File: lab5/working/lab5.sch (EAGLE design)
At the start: 29 parts, among them J1 ISP, U1 ATMEGA128RFA1, Y1 16MHz

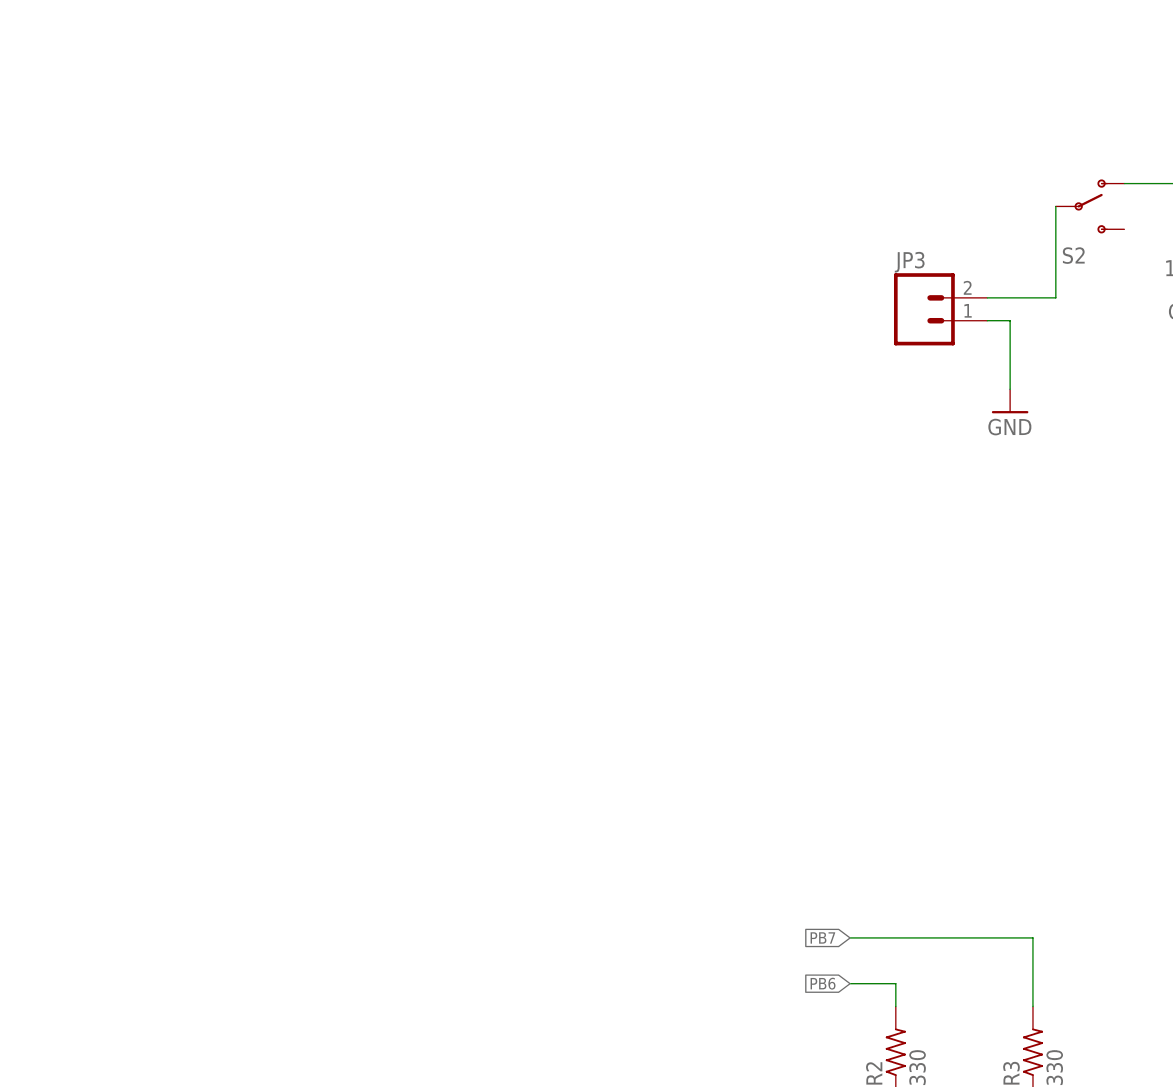
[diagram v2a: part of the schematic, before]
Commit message: added power IMU
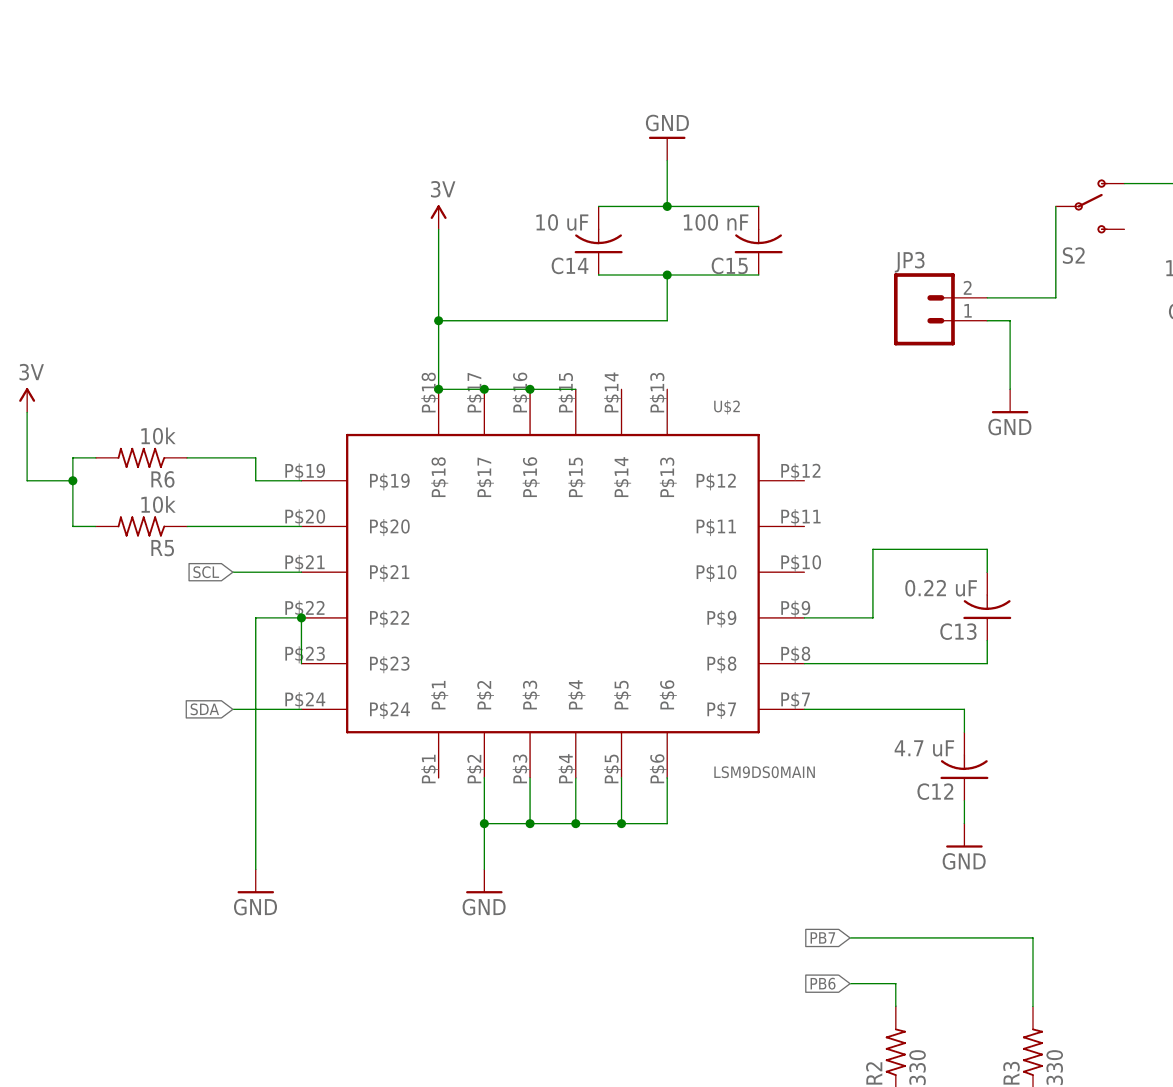
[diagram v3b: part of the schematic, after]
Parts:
- added C12: 4.7 uF, Lab5:C-USC0805
- added C13: 0.22 uF, Lab5:C-USC0805
- added C14: 10 uF, Lab5:C-USC0805
- added C15: 100 nF, Lab5:C-USC0805
- added R5, R6: 10k, Lab5:R-US_R0805
- added U$2: LSM9DS0MAIN, lab4:LSM9DS0MAIN
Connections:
- new net N$21: C12.2, U$2.P$7
- new net N$22: C13.2, U$2.P$9
- new net N$23: C13.1, U$2.P$8
- new net N$28: R5.1, U$2.P$20
- new net N$29: R6.1, U$2.P$19
- net 3.3V: now also C14.1, C15.1, R5.2, R6.2, U$2.P$15, U$2.P$16, U$2.P$17, U$2.P$18
- net GND: now also C12.1, C14.2, C15.2, U$2.P$2, U$2.P$22, U$2.P$23, U$2.P$3, U$2.P$4, U$2.P$5, U$2.P$6
- net SCL: now also U$2.P$21
- net SDA: now also U$2.P$24
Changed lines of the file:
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@@
 <part name="GND20" library="Lab5" deviceset="GND" device=""/>
 <part name="R4" library="Lab5" deviceset="R-US_" device="R0805" value="1k"/>
+<part name="U$2" library="lab4" deviceset="LSM9DS0" device="MAIN"/>
+<part name="P+4" library="Lab5" deviceset="3.3V" device="" value="3V"/>
+<part name="GND21" library="Lab5" deviceset="GND" device=""/>
+<part name="C12" library="Lab5" deviceset="C-US" device="C0805" value="4.7 uF"/>
+<part name="GND22" library="Lab5" deviceset="GND" device=""/>
+<part name="C13" library="Lab5" deviceset="C-US" device="C0805" value="0.22 uF"/>
+<part name="C14" library="Lab5" deviceset="C-US" device="C0805" value="10 uF"/>
+<part name="C15" library="Lab5" deviceset="C-US" device="C0805" value="100 nF"/>
+<part name="GND23" library="Lab5" deviceset="GND" device=""/>
+<part name="GND24" library="Lab5" deviceset="GND" device=""/>
+<part name="R5" library="Lab5" deviceset="R-US_" device="R0805" value="10k"/>
+<part name="R6" library="Lab5" deviceset="R-US_" device="R0805" value="10k"/>
+<part name="P+5" library="Lab5" deviceset="3.3V" device="" value="3V"/>
 </parts>
 <sheets>
@@
 <instance part="GND20" gate="1" x="-30.48" y="30.48"/>
 <instance part="R4" gate="G$1" x="-38.1" y="53.34" rot="R180"/>
+<instance part="U$2" gate="IMU" x="-165.1" y="7.62"/>
+<instance part="P+4" gate="G$1" x="-177.8" y="48.26"/>
+<instance part="GND21" gate="1" x="-172.72" y="-25.4"/>
+<instance part="C12" gate="G$1" x="-119.38" y="-12.7" rot="R180"/>
+<instance part="GND22" gate="1" x="-119.38" y="-20.32"/>
+<instance part="C13" gate="G$1" x="-116.84" y="5.08" rot="R180"/>
+<instance part="C14" gate="G$1" x="-160.02" y="45.72" rot="R180"/>
+<instance part="C15" gate="G$1" x="-142.24" y="45.72" rot="R180"/>
+<instance part="GND23" gate="1" x="-152.4" y="58.42" rot="R180"/>
+<instance part="GND24" gate="1" x="-198.12" y="-25.4"/>
+<instance part="R5" gate="G$1" x="-210.82" y="15.24" rot="R180"/>
+<instance part="R6" gate="G$1" x="-210.82" y="22.86" rot="R180"/>
+<instance part="P+5" gate="G$1" x="-223.52" y="27.94"/>
 </instances>
 <busses>
@@
 <wire x1="-30.48" y1="38.1" x2="-30.48" y2="33.02" width="0.1524" layer="91"/>
 </segment>
+<segment>
+<pinref part="U$2" gate="IMU" pin="P$6"/>
+<wire x1="-152.4" y1="-12.7" x2="-152.4" y2="-17.78" width="0.1524" layer="91"/>
+<pinref part="U$2" gate="IMU" pin="P$5"/>
+<wire x1="-157.48" y1="-12.7" x2="-157.48" y2="-17.78" width="0.1524" layer="91"/>
+<wire x1="-152.4" y1="-17.78" x2="-157.48" y2="-17.78" width="0.1524" layer="91"/>
+<pinref part="U$2" gate="IMU" pin="P$4"/>
+<wire x1="-162.56" y1="-12.7" x2="-162.56" y2="-17.78" width="0.1524" layer="91"/>
+<wire x1="-157.48" y1="-17.78" x2="-162.56" y2="-17.78" width="0.1524" layer="91"/>
+<junction x="-157.48" y="-17.78"/>
+<pinref part="U$2" gate="IMU" pin="P$3"/>
+<wire x1="-167.64" y1="-12.7" x2="-167.64" y2="-17.78" width="0.1524" layer="91"/>
+<wire x1="-162.56" y1="-17.78" x2="-167.64" y2="-17.78" width="0.1524" layer="91"/>
+<junction x="-162.56" y="-17.78"/>
+<pinref part="U$2" gate="IMU" pin="P$2"/>
+<wire x1="-172.72" y1="-12.7" x2="-172.72" y2="-17.78" width="0.1524" layer="91"/>
+<wire x1="-167.64" y1="-17.78" x2="-172.72" y2="-17.78" width="0.1524" layer="91"/>
+<junction x="-167.64" y="-17.78"/>
+<pinref part="GND21" gate="1" pin="GND"/>
+<wire x1="-172.72" y1="-17.78" x2="-172.72" y2="-22.86" width="0.1524" layer="91"/>
+<junction x="-172.72" y="-17.78"/>
+</segment>
+<segment>
+<pinref part="C12" gate="G$1" pin="1"/>
+<pinref part="GND22" gate="1" pin="GND"/>
+<wire x1="-119.38" y1="-15.24" x2="-119.38" y2="-17.78" width="0.1524" layer="91"/>
+</segment>
+<segment>
+<pinref part="C15" gate="G$1" pin="2"/>
+<pinref part="C14" gate="G$1" pin="2"/>
+<wire x1="-142.24" y1="50.8" x2="-152.4" y2="50.8" width="0.1524" layer="91"/>
+<wire x1="-152.4" y1="50.8" x2="-160.02" y2="50.8" width="0.1524" layer="91"/>
+<wire x1="-152.4" y1="50.8" x2="-152.4" y2="55.88" width="0.1524" layer="91"/>
+<junction x="-152.4" y="50.8"/>
+<pinref part="GND23" gate="1" pin="GND"/>
+</segment>
+<segment>
+<pinref part="U$2" gate="IMU" pin="P$23"/>
+<pinref part="U$2" gate="IMU" pin="P$22"/>
+<wire x1="-193.04" y1="0" x2="-193.04" y2="5.08" width="0.1524" layer="91"/>
+<wire x1="-193.04" y1="5.08" x2="-198.12" y2="5.08" width="0.1524" layer="91"/>
+<junction x="-193.04" y="5.08"/>
+<wire x1="-198.12" y1="5.08" x2="-198.12" y2="-22.86" width="0.1524" layer="91"/>
+<pinref part="GND24" gate="1" pin="GND"/>
+</segment>
 </net>
 <net name="A7" class="0">
@@
 <label x="-88.9" y="-25.4" size="1.27" layer="95" rot="R180" xref="yes"/>
 </segment>
+<segment>
+<pinref part="U$2" gate="IMU" pin="P$24"/>
+<wire x1="-193.04" y1="-5.08" x2="-200.66" y2="-5.08" width="0.1524" layer="91"/>
+<label x="-200.66" y="-5.08" size="1.27" layer="95" rot="R180" xref="yes"/>
+</segment>
 </net>
 <net name="SCL" class="0">
@@
 <wire x1="-83.82" y1="-22.86" x2="-88.9" y2="-22.86" width="0.1524" layer="91"/>
 <label x="-88.9" y="-22.86" size="1.27" layer="95" rot="R180" xref="yes"/>
+</segment>
+<segment>
+<pinref part="U$2" gate="IMU" pin="P$21"/>
+<wire x1="-193.04" y1="10.16" x2="-200.66" y2="10.16" width="0.1524" layer="91"/>
+<label x="-200.66" y="10.16" size="1.27" layer="95" rot="R180" xref="yes"/>
 </segment>
 </net>
@@
 <wire x1="-45.72" y1="53.34" x2="-43.18" y2="53.34" width="0.1524" layer="91"/>
 <junction x="-45.72" y="53.34"/>
+</segment>
+<segment>
+<pinref part="U$2" gate="IMU" pin="P$18"/>
+<wire x1="-177.8" y1="30.48" x2="-177.8" y2="38.1" width="0.1524" layer="91"/>
+<pinref part="P+4" gate="G$1" pin="3.3V"/>
+<pinref part="U$2" gate="IMU" pin="P$15"/>
+<pinref part="U$2" gate="IMU" pin="P$16"/>
+<wire x1="-177.8" y1="38.1" x2="-177.8" y2="48.26" width="0.1524" layer="91"/>
+<wire x1="-162.56" y1="30.48" x2="-167.64" y2="30.48" width="0.1524" layer="91"/>
+<pinref part="U$2" gate="IMU" pin="P$17"/>
+<wire x1="-167.64" y1="30.48" x2="-172.72" y2="30.48" width="0.1524" layer="91"/>
+<junction x="-167.64" y="30.48"/>
+<wire x1="-172.72" y1="30.48" x2="-177.8" y2="30.48" width="0.1524" layer="91"/>
+<junction x="-172.72" y="30.48"/>
+<junction x="-177.8" y="30.48"/>
+<wire x1="-177.8" y1="38.1" x2="-152.4" y2="38.1" width="0.1524" layer="91"/>
+<junction x="-177.8" y="38.1"/>
+<wire x1="-152.4" y1="38.1" x2="-152.4" y2="43.18" width="0.1524" layer="91"/>
+<pinref part="C14" gate="G$1" pin="1"/>
+<wire x1="-152.4" y1="43.18" x2="-160.02" y2="43.18" width="0.1524" layer="91"/>
+<pinref part="C15" gate="G$1" pin="1"/>
+<wire x1="-152.4" y1="43.18" x2="-142.24" y2="43.18" width="0.1524" layer="91"/>
+<junction x="-152.4" y="43.18"/>
+</segment>
+<segment>
+<pinref part="R6" gate="G$1" pin="2"/>
+<wire x1="-215.9" y1="22.86" x2="-218.44" y2="22.86" width="0.1524" layer="91"/>
+<wire x1="-218.44" y1="22.86" x2="-218.44" y2="20.32" width="0.1524" layer="91"/>
+<pinref part="R5" gate="G$1" pin="2"/>
+<wire x1="-218.44" y1="20.32" x2="-218.44" y2="15.24" width="0.1524" layer="91"/>
+<wire x1="-218.44" y1="15.24" x2="-215.9" y2="15.24" width="0.1524" layer="91"/>
+<wire x1="-218.44" y1="20.32" x2="-223.52" y2="20.32" width="0.1524" layer="91"/>
+<junction x="-218.44" y="20.32"/>
+<wire x1="-223.52" y1="20.32" x2="-223.52" y2="27.94" width="0.1524" layer="91"/>
+<pinref part="P+5" gate="G$1" pin="3.3V"/>
 </segment>
 </net>
@@
 </segment>
 </net>
+<net name="N$21" class="0">
+<segment>
+<pinref part="U$2" gate="IMU" pin="P$7"/>
+<wire x1="-137.16" y1="-5.08" x2="-119.38" y2="-5.08" width="0.1524" layer="91"/>
+<pinref part="C12" gate="G$1" pin="2"/>
+<wire x1="-119.38" y1="-5.08" x2="-119.38" y2="-7.62" width="0.1524" layer="91"/>
+</segment>
+</net>
+<net name="N$22" class="0">
+<segment>
+<pinref part="U$2" gate="IMU" pin="P$9"/>
+<wire x1="-137.16" y1="5.08" x2="-129.54" y2="5.08" width="0.1524" layer="91"/>
+<wire x1="-129.54" y1="5.08" x2="-129.54" y2="12.7" width="0.1524" layer="91"/>
+<pinref part="C13" gate="G$1" pin="2"/>
+<wire x1="-116.84" y1="10.16" x2="-116.84" y2="12.7" width="0.1524" layer="91"/>
+<wire x1="-116.84" y1="12.7" x2="-129.54" y2="12.7" width="0.1524" layer="91"/>
+</segment>
+</net>
+<net name="N$23" class="0">
+<segment>
+<pinref part="U$2" gate="IMU" pin="P$8"/>
+<wire x1="-137.16" y1="0" x2="-116.84" y2="0" width="0.1524" layer="91"/>
+<pinref part="C13" gate="G$1" pin="1"/>
+<wire x1="-116.84" y1="0" x2="-116.84" y2="2.54" width="0.1524" layer="91"/>
+</segment>
+</net>
+<net name="N$28" class="0">
+<segment>
+<pinref part="U$2" gate="IMU" pin="P$20"/>
+<pinref part="R5" gate="G$1" pin="1"/>
+<wire x1="-193.04" y1="15.24" x2="-205.74" y2="15.24" width="0.1524" layer="91"/>
+</segment>
+</net>
+<net name="N$29" class="0">
+<segment>
+<pinref part="U$2" gate="IMU" pin="P$19"/>
+<wire x1="-193.04" y1="20.32" x2="-198.12" y2="20.32" width="0.1524" layer="91"/>
+<wire x1="-198.12" y1="20.32" x2="-198.12" y2="22.86" width="0.1524" layer="91"/>
+<pinref part="R6" gate="G$1" pin="1"/>
+<wire x1="-198.12" y1="22.86" x2="-205.74" y2="22.86" width="0.1524" layer="91"/>
+</segment>
+</net>

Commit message: finished lab5
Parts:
- added JP4, JP5, JP6, JP7: (no value), Lab5:M02PTH
- added U$10, U$13, U$4, U$7: BAS16WS, lab4:BAS16WS
- added U$11, U$14, U$5, U$8: SI2302CDS, lab4:SI2302CDS
- added U$12, U$3, U$6, U$9: RCL0805, lab4:RCL0805
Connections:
- removed net N$10: C11.2, S2.O, U$1.EN, U$1.IN
- new net N$12: JP5.1, U$7.P$2, U$8.D3
- new net N$15: JP6.1, U$10.P$2, U$11.D3
- new net N$16: JP7.1, U$13.P$2, U$14.D3
- new net N$32: JP4.1, U$4.P$2, U$5.D3
- new net VBAT: C11.2, JP4.2, JP5.2, JP6.2, JP7.2, S2.O, U$1.EN, U$1.IN, U$10.P$1, U$13.P$1, U$4.P$1, U$7.P$1
- net GND: now also U$11.S2, U$12.P$2, U$14.S2, U$3.P$2, U$5.S2, U$6.P$2, U$8.S2, U$9.P$2
- net PB5: now also U$12.P$1, U$14.G1
- net PE3: now also U$6.P$1, U$8.G1
- net PE4: now also U$3.P$1, U$5.G1
- net PE5: now also U$11.G1, U$9.P$1

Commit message: added document info in frame
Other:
- note added: "Kirt Spotkaeff"
- note added: "Matt Asaro"
- moved on the sheet: A1, B1, C1, C10, C11, C12, C13, C14, C15, C2, C3, C4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

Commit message: fixed some ERC errors
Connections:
- new net N$10: C9.1, JP1.1
- net TX0: no longer C9.1, JP1.1
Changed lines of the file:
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@@
 <segment>
 <pinref part="U1" gate="G$1" pin="PADDLE"/>
-<wire x1="78.74" y1="-22.86" x2="83.82" y2="-22.86" width="0.1524" layer="91"/>
 <wire x1="83.82" y1="-22.86" x2="83.82" y2="-30.48" width="0.1524" layer="91"/>
 <pinref part="GND1" gate="1" pin="GND"/>
 <pinref part="U1" gate="G$1" pin="DVSS"/>
-<wire x1="78.74" y1="-20.32" x2="83.82" y2="-20.32" width="0.1524" layer="91"/>
-<wire x1="83.82" y1="-20.32" x2="83.82" y2="-22.86" width="0.1524" layer="91"/>
 <pinref part="U1" gate="G$1" pin="AVSS"/>
+<junction x="83.82" y="-20.32"/>
 <wire x1="78.74" y1="-17.78" x2="83.82" y2="-17.78" width="0.1524" layer="91"/>
 <wire x1="83.82" y1="-17.78" x2="83.82" y2="-20.32" width="0.1524" layer="91"/>
+<wire x1="83.82" y1="-20.32" x2="83.82" y2="-22.86" width="0.1524" layer="91"/>
+<junction x="83.82" y="-22.86"/>
+<wire x1="83.82" y1="-20.32" x2="78.74" y2="-20.32" width="0.1524" layer="91"/>
+<wire x1="83.82" y1="-22.86" x2="78.74" y2="-22.86" width="0.1524" layer="91"/>
 </segment>
 <segment>
@@
 <wire x1="22.86" y1="10.16" x2="17.78" y2="10.16" width="0.1524" layer="91"/>
 <label x="17.78" y="10.16" size="1.27" layer="95" rot="R180" xref="yes"/>
-</segment>
-<segment>
-<pinref part="JP1" gate="G$1" pin="1"/>
-<pinref part="C9" gate="G$1" pin="1"/>
-<wire x1="60.96" y1="114.3" x2="73.66" y2="114.3" width="0.1524" layer="91"/>
 </segment>
 <segment>
@@
 </segment>
 </net>
+<net name="N$10" class="0">
+<segment>
+<pinref part="C9" gate="G$1" pin="1"/>
+<pinref part="JP1" gate="G$1" pin="1"/>
+<wire x1="73.66" y1="114.3" x2="60.96" y2="114.3" width="0.1524" layer="91"/>
+</segment>
+</net>

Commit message: updated schematic to look nice
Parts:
- added C16: 1 uF, Lab5:C-USC0805
- JP3: value (none) -> Battery Terminal
- JP4: value (none) -> Motor4
- JP5: value (none) -> Motor3
- JP6: value (none) -> Motor2
- JP7: value (none) -> Motor1
- S2: value (none) -> Power Switch
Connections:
- removed net A0: U1.PF0(ADC0)
- removed net A1: U1.PF1(ADC1)
- removed net A2: U1.PF2(ADC2/DIG2)
- removed net A3: U1.PF3(ADC3/DIG4)
- removed net A4: U1.PF4(ADC4/TCK)
- removed net A5: U1.PF5(ADC5/TMS)
- removed net A6: U1.PF6(ADC6/TDO)
- removed net A7: U1.PF7(ADC7/TDI)
- removed net AREF: U1.AREF
- removed net CLKI: U1.CLKI
- removed net PB4: U1.PB4(OC2A/PCINT4)
- removed net PD4: U1.PD4(ICP1)
- removed net PD5: U1.PD5(XCK1)
- removed net PD6: U1.PD6(T1)
- removed net PD7: U1.PD7(T0)
- removed net PE2: U1.PE2(XCK0/AIN0)
- removed net PE6: U1.PE6(T3/INT6)
- removed net PE7: U1.PE7(ICP3/INT7/CLKO)
- removed net PG0: U1.PG0(DIG3)
- removed net PG1: U1.PG1(DIG1)
- removed net PG2: U1.PG2(AMR)
- removed net PG5: U1.PG5(OC0B)
- removed net RSTON: U1.RSTON
- removed net SSN: U1.PB0(SSN/PCINT0)
- removed net TST: U1.TST
- net 3.3V: now also C16.2
- net GND: now also C16.1
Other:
- note added: "IMU"
- note added: "ISP"
- note added: "MICRO-CONTROLLER"
- note added: "MOTORS"
- note added: "POWER"
- note added: "SERIAL"
- note added: "SERIAL -DEBUGGER"
- note added: "SWITCH"
- moved on the sheet: A1, B1, C1, C10, C11, C2, C3, C4, C5, C6, C7, C8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
